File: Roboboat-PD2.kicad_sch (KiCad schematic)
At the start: 27 parts, among them J1 12V, J10 Motor, J11 Motor, J12 Motor, J13 Motor, J14 5V, J15 14.4V, J2 Bucky, J3 Jetson, J4 Motor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

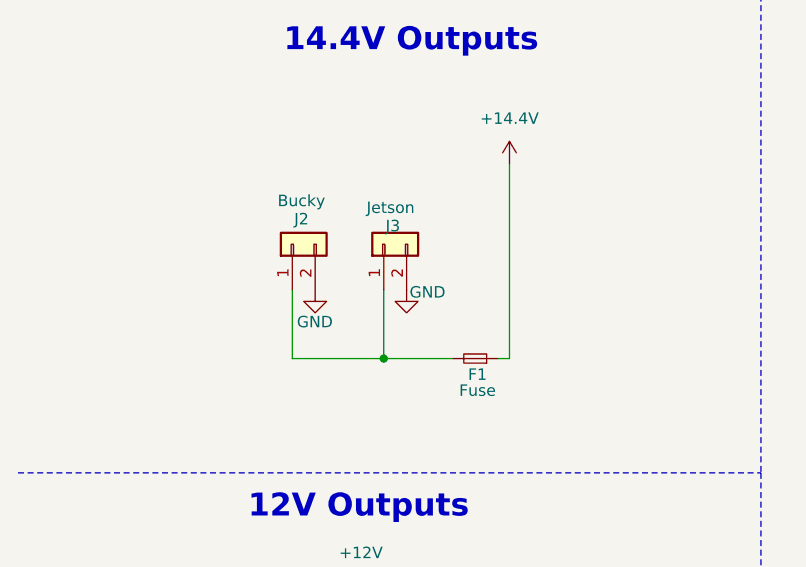
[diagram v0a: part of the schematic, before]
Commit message: move fuse
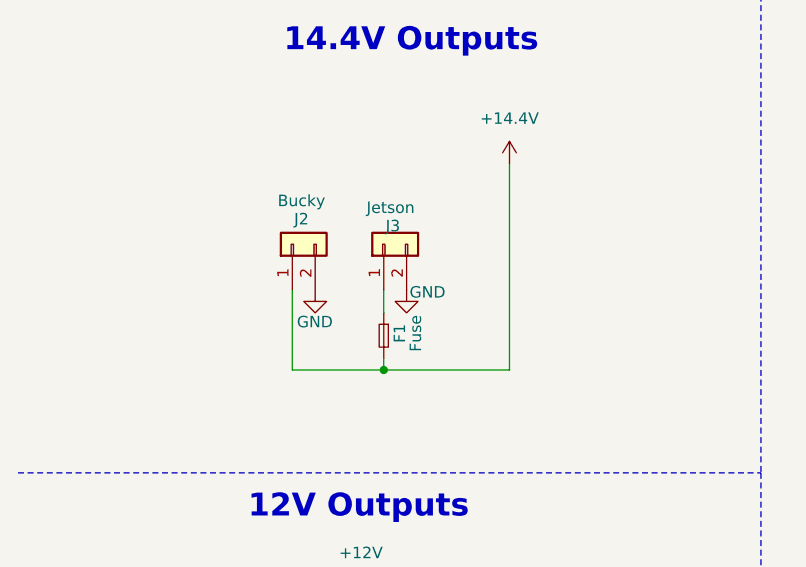
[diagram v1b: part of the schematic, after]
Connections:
- net +14.4V: now also F1.2, J2.1 (Pin_1); no longer F1.1
- new net: F1.1, J3.1 (Pin_1)
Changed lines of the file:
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@@
 	)
 	(junction
-		(at 52.07 63.5)
+		(at 52.07 64.77)
 		(diameter 0)
 		(color 0 0 0 0)
@@
 	(wire
 		(pts
-			(xy 41.91 63.5) (xy 52.07 63.5)
-		)
-		(stroke
-			(width 0)
-			(type default)
-		)
-	)
-	(wire
-		(pts
-			(xy 52.07 55.88) (xy 52.07 63.5)
+			(xy 41.91 64.77) (xy 52.07 64.77)
+		)
+		(stroke
+			(width 0)
+			(type default)
+		)
+	)
+	(wire
+		(pts
+			(xy 52.07 55.88) (xy 52.07 58.42)
 		)
 		(stroke
@@
 		)
 	)
+	(wire
+		(pts
+			(xy 52.07 64.77) (xy 52.07 63.5)
+		)
+		(stroke
+			(width 0)
+			(type default)
+		)
+	)
 	(polyline
 		(pts
@@
 	(wire
 		(pts
-			(xy 66.04 41.91) (xy 66.04 63.5)
+			(xy 66.04 41.91) (xy 66.04 64.77)
 		)
 		(stroke
@@
 	(wire
 		(pts
-			(xy 41.91 55.88) (xy 41.91 63.5)
+			(xy 41.91 55.88) (xy 41.91 64.77)
 		)
 		(stroke
@@
 		)
 	)
-	(wire
-		(pts
-			(xy 64.77 63.5) (xy 66.04 63.5)
-		)
-		(stroke
-			(width 0)
-			(type default)
-		)
-	)
 	(polyline
 		(pts
@@
 	(wire
 		(pts
-			(xy 52.07 63.5) (xy 59.69 63.5)
+			(xy 52.07 64.77) (xy 66.04 64.77)
 		)
 		(stroke
@@
 	)
 	(symbol
+		(lib_id "Device:Fuse_Small")
+		(at 52.07 60.96 270)
+		(unit 1)
+		(exclude_from_sim no)
+		(in_bom yes)
+		(on_board yes)
+		(dnp no)
+		(property "Reference" "F1"
+			(at 53.848 60.706 0)
+			(effects
+				(font
+					(size 1.27 1.27)
+				)
+			)
+		)
+		(property "Value" "Fuse"
+			(at 55.626 60.706 0)
+			(effects
+				(font
+					(size 1.27 1.27)
+				)
+			)
+		)
+		(property "Footprint" "footprints:0ZCG_BEL"
+			(at 52.07 60.96 0)
+			(effects
+				(font
+					(size 1.27 1.27)
+				)
+				(hide yes)
+			)
+		)
+		(property "Datasheet" "https://www.belfuse.com/resources/datasheets/circuitprotection/ds-cp-0zcg-series.pdf"
+			(at 52.07 60.96 0)
+			(effects
+				(font
+					(size 1.27 1.27)
+				)
+				(hide yes)
+			)
+		)
+		(property "Description" "Fuse, small symbol"
+			(at 52.07 60.96 0)
+			(effects
+				(font
+					(size 1.27 1.27)
+				)
+				(hide yes)
+			)
+		)
+		(pin "1"
+		)
+		(pin "2"
+		)
+		(instances
+			(project "Roboboat-PD2"
+				(path "/9a1496f4-7cef-4d33-8239-9c2f43ceb177"
+					(reference "F1")
+					(unit 1)
+				)
+			)
+		)
+	)
+	(symbol
 		(lib_id "power:GND")
 		(at 57.15 140.97 0)
@@
 					(unit 1)
 				)
-			)
-		)
-	)
-	(symbol
-		(lib_id "Device:Fuse_Small")
-		(at 62.23 63.5 180)
-		(unit 1)
-		(exclude_from_sim no)
-		(in_bom yes)
-		(on_board yes)
-		(dnp no)
-		(property "Reference" "F1"
-			(at 62.484 65.278 0)
-			(effects
-				(font
-					(size 1.27 1.27)
-				)
-			)
-		)
-		(property "Value" "Fuse"
-			(at 62.484 67.056 0)
-			(effects
-				(font
-					(size 1.27 1.27)
-				)
-			)
-		)
-		(property "Footprint" "footprints:0ZCG_BEL"
-			(at 62.23 63.5 0)
-			(effects
-				(font
-					(size 1.27 1.27)
-				)
-				(hide yes)
-			)
-		)
-		(property "Datasheet" "https://www.belfuse.com/resources/datasheets/circuitprotection/ds-cp-0zcg-series.pdf"
-			(at 62.23 63.5 0)
-			(effects
-				(font
-					(size 1.27 1.27)
-				)
-				(hide yes)
-			)
-		)
-		(property "Description" "Fuse, small symbol"
-			(at 62.23 63.5 0)
-			(effects
-				(font
-					(size 1.27 1.27)
-				)
-				(hide yes)
-			)
-		)
-		(pin "1"
-		)
-		(pin "2"
-		)
-		(instances
-			(project "Roboboat-PD2"
-				(path "/9a1496f4-7cef-4d33-8239-9c2f43ceb177"
-					(reference "F1")
-					(unit 1)
-				)

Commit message: fix footprints
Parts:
- C2, C3: footprint footprints:CL05B104KA5NNNC -> footprints:CAP_CL05B104KA5NNNC_SAM
- R1: footprint footprints:RC0402N_PAN -> footprints:RC0402N_YAG
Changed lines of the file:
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@@
 			)
 		)
-		(property "Footprint" "footprints:RC0402N_PAN"
+		(property "Footprint" "footprints:RC0402N_YAG"
 			(at 122.174 42.926 90)
 			(effects
@@
 			)
 		)
-		(property "Footprint" "footprints:CL05B104KA5NNNC"
+		(property "Footprint" "footprints:CAP_CL05B104KA5NNNC_SAM"
 			(at 121.92 90.17 0)
 			(effects
@@
 			)
 		)
-		(property "Footprint" "footprints:CL05B104KA5NNNC"
+		(property "Footprint" "footprints:CAP_CL05B104KA5NNNC_SAM"
 			(at 161.29 55.88 0)
 			(effects

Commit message: change fuse
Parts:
- F1: footprint footprints:0ZCG_BEL -> footprints:FUSE_0ZCF0075AF2C
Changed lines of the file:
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@@
 			)
 		)
-		(property "Footprint" "footprints:0ZCG_BEL"
+		(property "Footprint" "footprints:FUSE_0ZCF0075AF2C"
 			(at 52.07 60.96 0)
 			(effects
@@
 			)
 		)
-		(property "Datasheet" "https://www.belfuse.com/resources/datasheets/circuitprotection/ds-cp-0zcg-series.pdf"
+		(property "Datasheet" "https://www.belfuse.com/resources/datasheets/circuitprotection/ds-cp-0zcf-series.pdf"
 			(at 52.07 60.96 0)
 			(effects

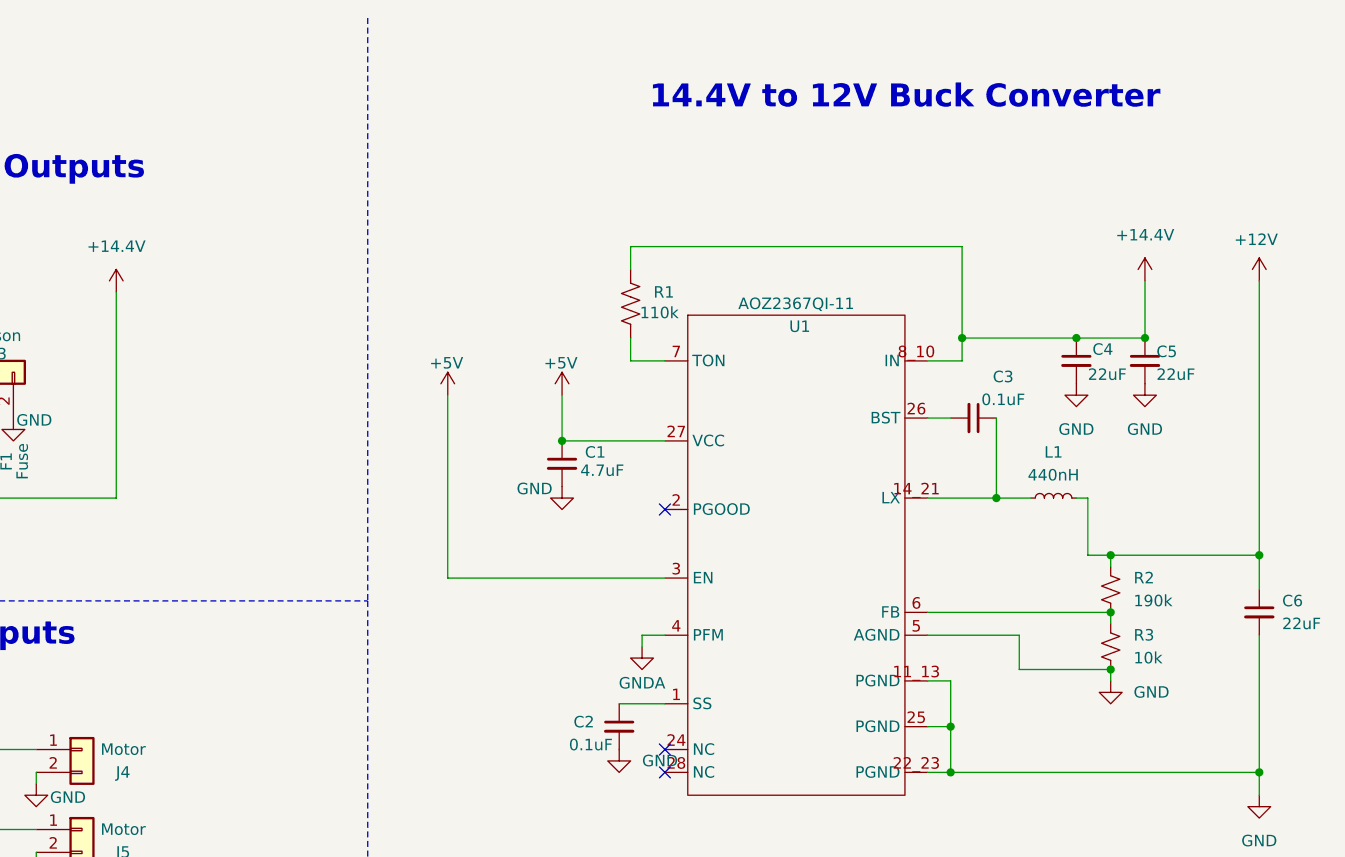
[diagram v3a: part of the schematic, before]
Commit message: fix capacitor and resistor values and sizes
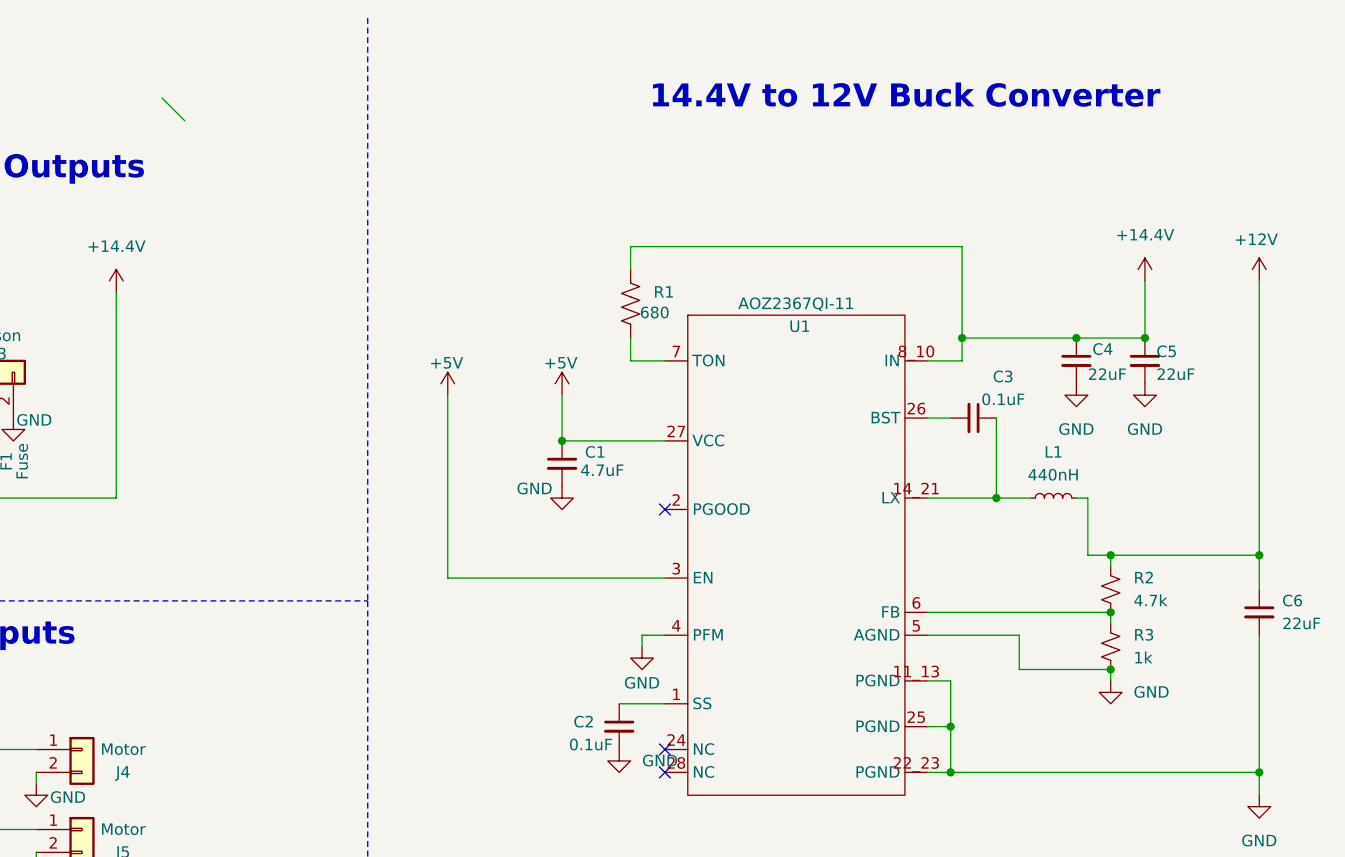
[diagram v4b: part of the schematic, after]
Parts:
- C2, C3: footprint footprints:CAP_CL05B104KA5NNNC_SAM -> Capacitor_SMD:C_1206_3216Metric
- R1: value 110k -> 680; footprint footprints:RC0402N_YAG -> Resistor_SMD:R_0805_2012Metric
- R2: value 190k -> 4.7k; footprint footprints:RES_TTD1002F_KOA -> Resistor_SMD:R_0805_2012Metric
- R3: value 10k -> 1k; footprint footprints:RES_TTD1002F_KOA -> Resistor_SMD:R_0805_2012Metric
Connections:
- net GNDA is gone; now on net GND: U1.4 (PFM)
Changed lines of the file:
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@@
 		(at 127 92.71)
 	)
+	(bus_entry
+		(at 71.12 20.32)
+		(size 2.54 2.54)
+		(stroke
+			(width 0)
+			(type default)
+		)
+	)
 	(wire
 		(pts
@@
 			)
 		)
-		(property "Value" "190k"
+		(property "Value" "4.7k"
 			(at 179.07 76.1999 0)
 			(effects
@@
 			)
 		)
-		(property "Footprint" "footprints:RES_TTD1002F_KOA"
+		(property "Footprint" "Resistor_SMD:R_0805_2012Metric"
 			(at 176.53 74.93 0)
 			(effects
@@
 			)
 		)
-		(property "Value" "110k"
+		(property "Value" "680"
 			(at 124.206 44.196 0)
 			(effects
@@
 			)
 		)
-		(property "Footprint" "footprints:RC0402N_YAG"
+		(property "Footprint" "Resistor_SMD:R_0805_2012Metric"
 			(at 122.174 42.926 90)
 			(effects
@@
 			)
 		)
-		(property "Footprint" "footprints:CAP_CL05B104KA5NNNC_SAM"
+		(property "Footprint" "Capacitor_SMD:C_1206_3216Metric"
 			(at 121.92 90.17 0)
 			(effects
@@
 			)
 		)
-		(property "Value" "10k"
+		(property "Value" "1k"
 			(at 179.07 82.5499 0)
 			(effects
@@
 			)
 		)
-		(property "Footprint" "footprints:RES_TTD1002F_KOA"
+		(property "Footprint" "Resistor_SMD:R_0805_2012Metric"
 			(at 176.53 81.28 0)
 			(effects
@@
 			)
 		)
-		(property "Value" "GNDA"
+		(property "Value" "GND"
 			(at 124.46 85.344 0)
 			(effects
@@
 			)
 		)
-		(property "Footprint" "footprints:CAP_CL05B104KA5NNNC_SAM"
+		(property "Footprint" "Capacitor_SMD:C_1206_3216Metric"
 			(at 161.29 55.88 0)
 			(effects

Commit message: tweak silkscreen
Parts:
- C4, C5: footprint footprints:CAP_CL31_SAM -> Capacitor_SMD:C_1206_3216Metric
- C6: footprint footprints:CAP_CL32_SAM -> Capacitor_SMD:C_1206_3216Metric
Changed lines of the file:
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@@
 			)
 		)
-		(property "Footprint" "footprints:CAP_CL31_SAM"
+		(property "Footprint" "Capacitor_SMD:C_1206_3216Metric"
 			(at 172.72 49.53 0)
 			(effects
@@
 			)
 		)
-		(property "Footprint" "footprints:CAP_CL31_SAM"
+		(property "Footprint" "Capacitor_SMD:C_1206_3216Metric"
 			(at 180.34 49.53 0)
 			(effects
@@
 			)
 		)
-		(property "Footprint" "footprints:CAP_CL32_SAM"
+		(property "Footprint" "Capacitor_SMD:C_1206_3216Metric"
 			(at 193.04 77.47 0)
 			(effects

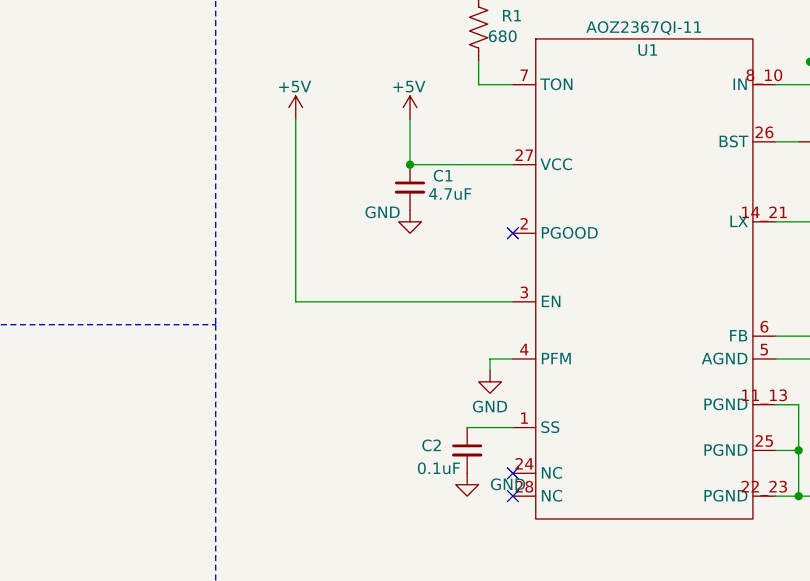
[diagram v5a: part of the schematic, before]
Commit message: tie PFM high, break out PGOOD
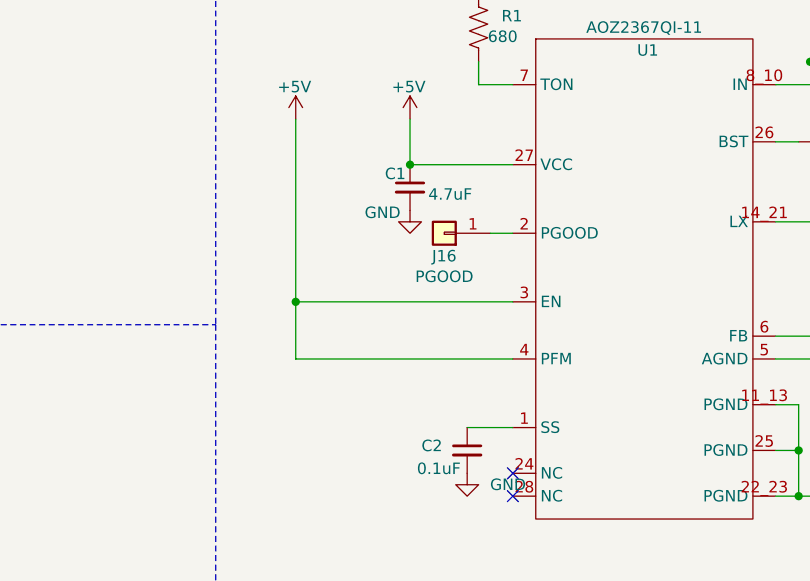
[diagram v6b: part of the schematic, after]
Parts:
- added J16: PGOOD, Connector_JST:JST_XH_B1B-XH-AM_1x01_P2.50mm_Vertical, symbol Connector_Generic:Conn_01x01
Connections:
- net +5V: now also U1.4 (PFM)
- net GND: no longer U1.4 (PFM)
- net at U1.2 (PGOOD): now also J16.1 (Pin_1)
- no-connect marks 3 -> 2
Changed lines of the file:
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@@
 	)
 	(junction
+		(at 102.87 73.66)
+		(diameter 0)
+		(color 0 0 0 0)
+	)
+	(junction
 		(at 49.53 119.38)
 		(diameter 0)
@@
 	)
 	(no_connect
-		(at 127 66.04)
-	)
-	(no_connect
 		(at 127 95.25)
 	)
@@
 	(wire
 		(pts
+			(xy 124.46 66.04) (xy 127 66.04)
+		)
+		(stroke
+			(width 0)
+			(type default)
+		)
+	)
+	(wire
+		(pts
 			(xy 49.53 172.72) (xy 57.15 172.72)
 		)
@@
 	(wire
 		(pts
-			(xy 124.46 80.01) (xy 127 80.01)
+			(xy 193.04 80.01) (xy 193.04 95.25)
 		)
 		(stroke
@@
 	(wire
 		(pts
-			(xy 193.04 80.01) (xy 193.04 95.25)
+			(xy 163.83 55.88) (xy 163.83 64.77)
 		)
 		(stroke
@@
 	(wire
 		(pts
-			(xy 163.83 55.88) (xy 163.83 64.77)
+			(xy 123.19 39.37) (xy 123.19 36.83)
 		)
 		(stroke
@@
 	(wire
 		(pts
-			(xy 123.19 39.37) (xy 123.19 36.83)
+			(xy 52.07 64.77) (xy 52.07 63.5)
 		)
 		(stroke
@@
 	(wire
 		(pts
-			(xy 52.07 64.77) (xy 52.07 63.5)
+			(xy 102.87 73.66) (xy 102.87 80.01)
 		)
 		(stroke
@@
 	(wire
 		(pts
-			(xy 124.46 81.28) (xy 124.46 80.01)
+			(xy 115.57 58.42) (xy 127 58.42)
 		)
 		(stroke
@@
 	(wire
 		(pts
-			(xy 115.57 58.42) (xy 127 58.42)
+			(xy 102.87 53.34) (xy 102.87 73.66)
 		)
 		(stroke
@@
 	(wire
 		(pts
+			(xy 102.87 80.01) (xy 127 80.01)
+		)
+		(stroke
+			(width 0)
+			(type default)
+		)
+	)
+	(wire
+		(pts
 			(xy 39.37 102.87) (xy 31.75 102.87)
 		)
@@
 		)
 	)
-	(wire
-		(pts
-			(xy 102.87 53.34) (xy 102.87 73.66)
-		)
-		(stroke
-			(width 0)
-			(type default)
-		)
-	)
 	(polyline
 		(pts
@@
 	)
 	(symbol
+		(lib_id "power:+1V1")
+		(at 115.57 53.34 0)
+		(unit 1)
+		(exclude_from_sim no)
+		(in_bom yes)
+		(on_board yes)
+		(dnp no)
+		(property "Reference" "#PWR019"
+			(at 115.57 57.15 0)
+			(effects
+				(font
+					(size 1.27 1.27)
+				)
+				(hide yes)
+			)
+		)
+		(property "Value" "+5V"
+			(at 113.538 49.784 0)
+			(effects
+				(font
+					(size 1.27 1.27)
+				)
+				(justify left)
+			)
+		)
+		(property "Footprint" ""
+			(at 115.57 53.34 0)
+			(effects
+				(font
+					(size 1.27 1.27)
+				)
+				(hide yes)
+			)
+		)
+		(property "Datasheet" ""
+			(at 115.57 53.34 0)
+			(effects
+				(font
+					(size 1.27 1.27)
+				)
+				(hide yes)
+			)
+		)
+		(property "Description" "Power symbol creates a global label with name \"+1V1\""
+			(at 115.57 53.34 0)
+			(effects
+				(font
+					(size 1.27 1.27)
+				)
+				(hide yes)
+			)
+		)
+		(pin "1"
+		)
+		(instances
+			(project "Roboboat-PD2"
+				(path "/9a1496f4-7cef-4d33-8239-9c2f43ceb177"
+					(reference "#PWR019")
+					(unit 1)
+				)
+			)
+		)
+	)
+	(symbol
 		(lib_id "power:GNDA")
 		(at 121.92 92.71 0)
@@
 	)
 	(symbol
-		(lib_id "power:+1V1")
-		(at 115.57 53.34 0)
-		(unit 1)
-		(exclude_from_sim no)
-		(in_bom yes)
-		(on_board yes)
-		(dnp no)
-		(property "Reference" "#PWR019"
-			(at 115.57 57.15 0)
-			(effects
-				(font
-					(size 1.27 1.27)
-				)
-				(hide yes)
-			)
-		)
-		(property "Value" "+5V"
-			(at 113.538 49.784 0)
-			(effects
-				(font
-					(size 1.27 1.27)
-				)
-				(justify left)
-			)
-		)
-		(property "Footprint" ""
-			(at 115.57 53.34 0)
-			(effects
-				(font
-					(size 1.27 1.27)
-				)
-				(hide yes)
-			)
-		)
-		(property "Datasheet" ""
-			(at 115.57 53.34 0)
-			(effects
-				(font
-					(size 1.27 1.27)
-				)
-				(hide yes)
-			)
-		)
-		(property "Description" "Power symbol creates a global label with name \"+1V1\""
-			(at 115.57 53.34 0)
-			(effects
-				(font
-					(size 1.27 1.27)
-				)
-				(hide yes)
-			)
-		)
-		(pin "1"
-		)
-		(instances
-			(project "Roboboat-PD2"
-				(path "/9a1496f4-7cef-4d33-8239-9c2f43ceb177"
-					(reference "#PWR019")
-					(unit 1)
-				)
-			)
-		)
-	)
-	(symbol
 		(lib_id "power:GND")
 		(at 57.15 158.75 0)
@@
 	)
 	(symbol
-		(lib_id "power:GNDA")
-		(at 124.46 81.28 0)
+		(lib_id "power:GND")
+		(at 57.15 176.53 0)
 		(unit 1)
 		(exclude_from_sim no)
@@
 		(on_board yes)
 		(dnp no)
-		(property "Reference" "#PWR024"
-			(at 124.46 87.63 0)
+		(property "Reference" "#PWR014"
+			(at 57.15 182.88 0)
 			(effects
 				(font
@@
 		)
 		(property "Value" "GND"
-			(at 124.46 85.344 0)
+			(at 58.674 178.054 0)
 			(effects
 				(font
 					(size 1.27 1.27)
 				)
+				(justify left)
 			)
 		)
 		(property "Footprint" ""
-			(at 124.46 81.28 0)
+			(at 57.15 176.53 0)
 			(effects
 				(font
@@
 		)
 		(property "Datasheet" ""
-			(at 124.46 81.28 0)
+			(at 57.15 176.53 0)
 			(effects
 				(font
@@
 			)
 		)
-		(property "Description" "Power symbol creates a global label with name \"GNDA\" , analog ground"
-			(at 124.46 81.28 0)
+		(property "Description" "Power symbol creates a global label with name \"GND\" , ground"
+			(at 57.15 176.53 0)
 			(effects
 				(font
@@
 			(project "Roboboat-PD2"
 				(path "/9a1496f4-7cef-4d33-8239-9c2f43ceb177"
-					(reference "#PWR024")
+					(reference "#PWR014")
 					(unit 1)
 				)
@@
 	)
 	(symbol
-		(lib_id "power:GND")
-		(at 57.15 176.53 0)
+		(lib_id "Connector_Generic:Conn_01x01")
+		(at 119.38 66.04 180)
 		(unit 1)
 		(exclude_from_sim no)
@@
 		(on_board yes)
 		(dnp no)
-		(property "Reference" "#PWR014"
-			(at 57.15 182.88 0)
+		(property "Reference" "J16"
+			(at 119.38 68.58 0)
 			(effects
 				(font
 					(size 1.27 1.27)
 				)
-				(hide yes)
 			)
 		)
-		(property "Value" "GND"
-			(at 58.674 178.054 0)
+		(property "Value" "PGOOD"
+			(at 119.38 70.866 0)
 			(effects
 				(font
 					(size 1.27 1.27)
 				)
-				(justify left)
 			)
 		)
-		(property "Footprint" ""
-			(at 57.15 176.53 0)
+		(property "Footprint" "Connector_JST:JST_XH_B1B-XH-AM_1x01_P2.50mm_Vertical"
+			(at 119.38 66.04 0)
 			(effects
 				(font
@@
 			)
 		)
-		(property "Datasheet" ""
-			(at 57.15 176.53 0)
+		(property "Datasheet" "~"
+			(at 119.38 66.04 0)
 			(effects
 				(font
@@
 			)
 		)
-		(property "Description" "Power symbol creates a global label with name \"GND\" , ground"
-			(at 57.15 176.53 0)
+		(property "Description" "Generic connector, single row, 01x01, script generated (kicad-library-utils/schlib/autogen/connector/)"
+			(at 119.38 66.04 0)
 			(effects
 				(font
@@
 		)
 		(instances
-			(project "Roboboat-PD2"
+			(project ""
 				(path "/9a1496f4-7cef-4d33-8239-9c2f43ceb177"
-					(reference "#PWR014")
+					(reference "J16")
 					(unit 1)
 				)
@@
 		(dnp no)
 		(property "Reference" "C1"
-			(at 118.11 59.6962 0)
+			(at 112.776 59.436 0)
 			(effects
 				(font

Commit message: rearrange board
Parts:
- added SW2: Jumper, Connector_PinHeader_1.00mm:PinHeader_1x02_P1.00mm_Vertical, symbol Switch:SW_SPST
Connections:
- net +5V: now also SW2.2 (B); no longer C1.1, U1.27 (VCC), U1.3 (EN), U1.4 (PFM)
- new net: C1.1, SW2.1 (A), U1.27 (VCC), U1.3 (EN), U1.4 (PFM)
